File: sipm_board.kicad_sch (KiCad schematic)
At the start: 17 parts, among them J5 *, J6 *, Q3 MMBT5088LT1G, Q4 MMBT5088LT1G, U9 MICROFC-60035-SMT-TR1

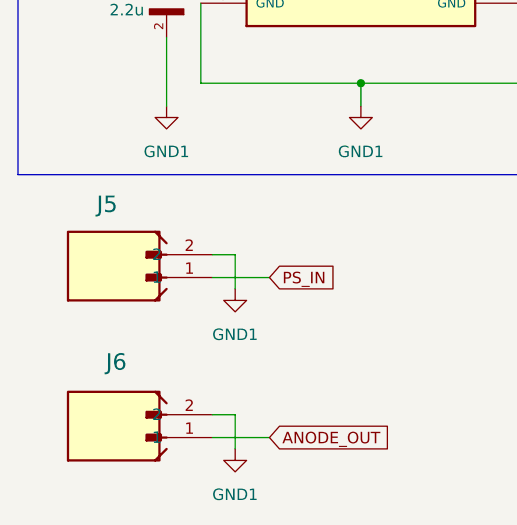
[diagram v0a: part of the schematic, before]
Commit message: Corrected labels
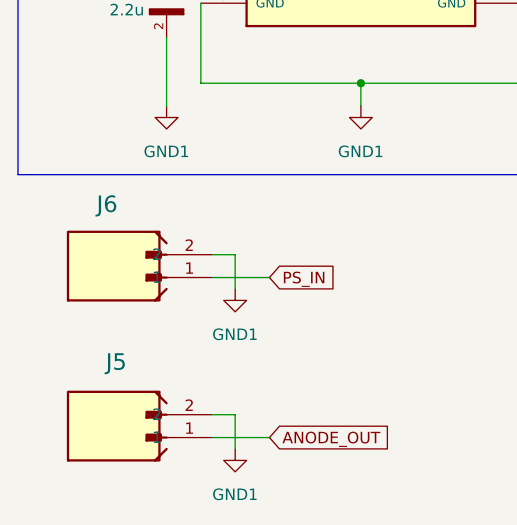
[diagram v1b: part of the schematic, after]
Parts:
- renumbered J6 to J5, J5 to J6
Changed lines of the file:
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@@
 		(on_board yes)
 		(dnp no)
-		(property "Reference" "J6"
+		(property "Reference" "J5"
 			(at 94.742 140.208 0)
 			(effects
@@
 			(project "gamma-spectrometer"
 				(path "/1fc9c372-472b-46ca-8d3b-f4aefe31a8be/1929b78d-718a-49ce-a44a-01f5c50b8f35"
-					(reference "J6")
+					(reference "J5")
 					(unit 1)
 				)
@@
 		(on_board yes)
 		(dnp no)
-		(property "Reference" "J5"
+		(property "Reference" "J6"
 			(at 93.726 122.682 0)
 			(effects
@@
 			(project "gamma-spectrometer"
 				(path "/1fc9c372-472b-46ca-8d3b-f4aefe31a8be/1929b78d-718a-49ce-a44a-01f5c50b8f35"
-					(reference "J5")
+					(reference "J6")
 					(unit 1)
 				)

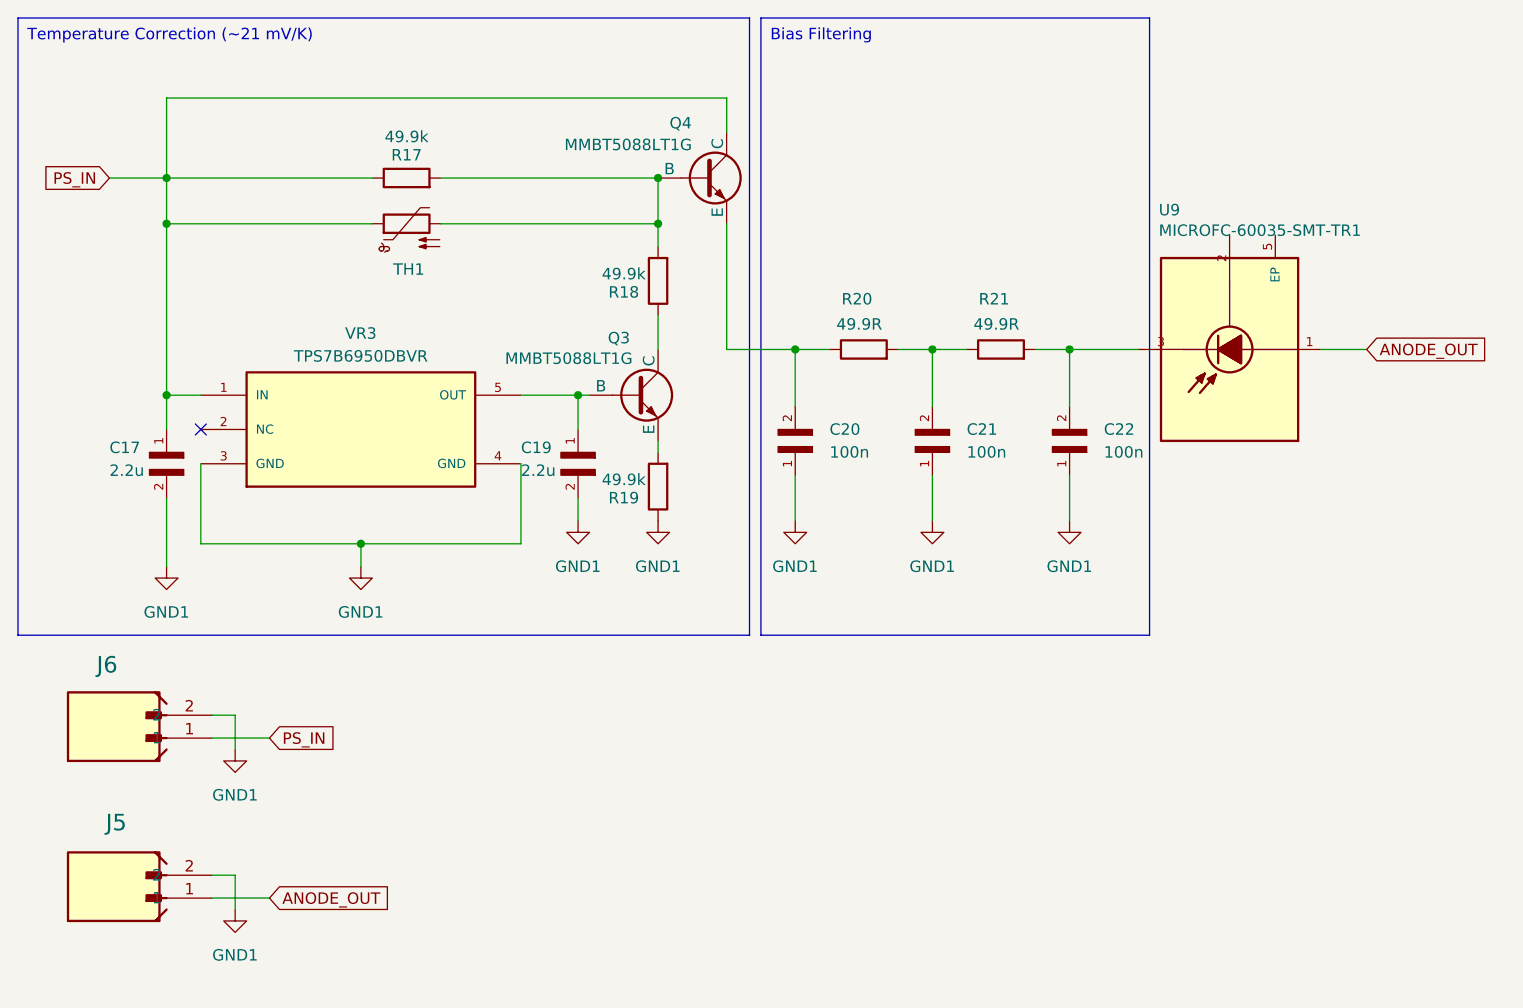
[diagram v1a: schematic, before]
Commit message: Added gain regulator. MHF3 connector for signal line.
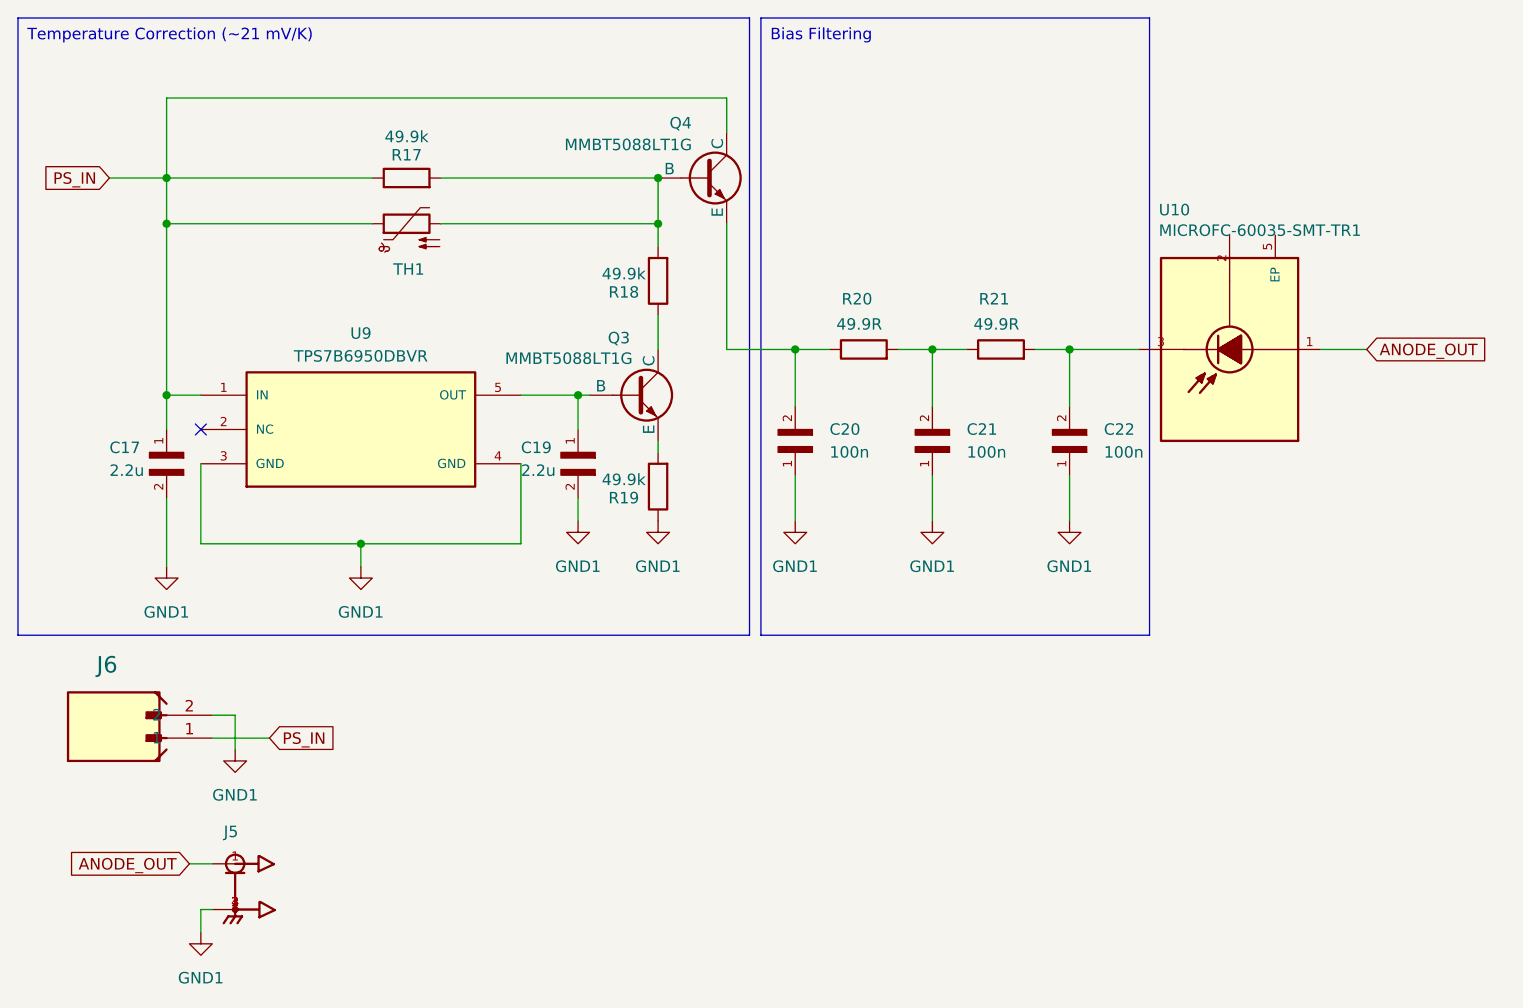
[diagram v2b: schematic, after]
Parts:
- removed J5: *, B2B-PH-K-S_LF__SN_:JST_B2B-PH-K-S(LF)(SN), symbol B2B-PH-K-S_LF__SN_:B2B-PH-K-S(LF)(SN)
- added J5: 20449-001E-03, 20449-001E-03:IPEX_20449-001E-03, symbol 20449-001E-03:20449-001E-03
- renumbered U9 to U10, VR3 to U9
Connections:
- net ANODE_OUT: now also J5.1
- net GND1: now also J5.2, J5.3, J5.4
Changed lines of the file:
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@@
+	(wire
+		(pts
+			(xy 102.87 144.78) (xy 105.41 144.78)
+		)
+		(stroke
+			(width 0)
+			(type default)
+		)
+	)
 	(wire
 		(pts
@@
 	(wire
 		(pts
-			(xy 107.95 146.05) (xy 107.95 149.86)
+			(xy 104.14 152.4) (xy 104.14 149.86)
 		)
 		(stroke
@@
 	(wire
 		(pts
-			(xy 111.76 148.59) (xy 105.41 148.59)
-		)
-		(stroke
-			(width 0)
-			(type default)
-		)
-	)
-	(wire
-		(pts
 			(xy 100.33 92.71) (xy 104.14 92.71)
 		)
@@
 	(wire
 		(pts
-			(xy 107.95 146.05) (xy 105.41 146.05)
-		)
-		(stroke
-			(width 0)
-			(type default)
-		)
-	)
-	(wire
-		(pts
 			(xy 200.66 87.63) (xy 208.28 87.63)
 		)
@@
 		(pts
 			(xy 104.14 109.22) (xy 121.92 109.22)
+		)
+		(stroke
+			(width 0)
+			(type default)
+		)
+	)
+	(wire
+		(pts
+			(xy 104.14 149.86) (xy 105.41 149.86)
 		)
 		(stroke
@@
 	(global_label "ANODE_OUT"
 		(shape input)
-		(at 111.76 148.59 0)
+		(at 102.87 144.78 180)
 		(fields_autoplaced yes)
 		(effects
@@
 				(size 1.27 1.27)
 			)
-			(justify left)
+			(justify right)
 		)
 		(property "Intersheetrefs" "${INTERSHEET_REFS}"
-			(at 125.51 148.59 0)
-			(effects
-				(font
-					(size 1.27 1.27)
-				)
-				(justify left)
+			(at 89.12 144.78 0)
+			(effects
+				(font
+					(size 1.27 1.27)
+				)
+				(justify right)
 				(hide yes)
 			)
@@
 				(justify left)
 				(hide yes)
+			)
+		)
+	)
+	(symbol
+		(lib_id "20449-001E-03:20449-001E-03")
+		(at 107.95 147.32 0)
+		(unit 1)
+		(exclude_from_sim no)
+		(in_bom yes)
+		(on_board yes)
+		(dnp no)
+		(property "Reference" "J5"
+			(at 106.68 141.224 0)
+			(effects
+				(font
+					(size 1.27 1.27)
+				)
+				(justify left)
+			)
+		)
+		(property "Value" "20449-001E-03"
+			(at 114.3 148.8439 0)
+			(effects
+				(font
+					(size 1.27 1.27)
+				)
+				(justify left)
+				(hide yes)
+			)
+		)
+		(property "Footprint" "20449-001E-03:IPEX_20449-001E-03"
+			(at 107.95 147.32 0)
+			(effects
+				(font
+					(size 1.27 1.27)
+				)
+				(justify bottom)
+				(hide yes)
+			)
+		)
+		(property "Datasheet" ""
+			(at 107.95 147.32 0)
+			(effects
+				(font
+					(size 1.27 1.27)
+				)
+				(hide yes)
+			)
+		)
+		(property "Description" ""
+			(at 107.95 147.32 0)
+			(effects
+				(font
+					(size 1.27 1.27)
+				)
+				(hide yes)
+			)
+		)
+		(property "MF" "I-PEX"
+			(at 107.95 147.32 0)
+			(effects
+				(font
+					(size 1.27 1.27)
+				)
+				(justify bottom)
+				(hide yes)
+			)
+		)
+		(property "Description_1" "\n                        \n                            1 POS Vertical SMD Small form factor with big performance through 6 GHz connector, RF, micro-coaxial MHF 4 Receptacle\n                        \n"
+			(at 107.95 147.32 0)
+			(effects
+				(font
+					(size 1.27 1.27)
+				)
+				(justify bottom)
+				(hide yes)
+			)
+		)
+		(property "Package" "None"
+			(at 107.95 147.32 0)
+			(effects
+				(font
+					(size 1.27 1.27)
+				)
+				(justify bottom)
+				(hide yes)
+			)
+		)
+		(property "Price" "None"
+			(at 107.95 147.32 0)
+			(effects
+				(font
+					(size 1.27 1.27)
+				)
+				(justify bottom)
+				(hide yes)
+			)
+		)
+		(property "Check_prices" "https://www.snapeda.com/parts/20449-001E-03/I-PEX/view-part/?ref=eda"
+			(at 107.95 147.32 0)
+			(effects
+				(font
+					(size 1.27 1.27)
+				)
+				(justify bottom)
+				(hide yes)
+			)
+		)
+		(property "PARTREV" "5"
+			(at 107.95 147.32 0)
+			(effects
+				(font
+					(size 1.27 1.27)
+				)
+				(justify bottom)
+				(hide yes)
+			)
+		)
+		(property "SnapEDA_Link" "https://www.snapeda.com/parts/20449-001E-03/I-PEX/view-part/?ref=snap"
+			(at 107.95 147.32 0)
+			(effects
+				(font
+					(size 1.27 1.27)
+				)
+				(justify bottom)
+				(hide yes)
+			)
+		)
+		(property "MP" "20449-001E-03"
+			(at 107.95 147.32 0)
+			(effects
+				(font
+					(size 1.27 1.27)
+				)
+				(justify bottom)
+				(hide yes)
+			)
+		)
+		(property "Availability" "In Stock"
+			(at 107.95 147.32 0)
+			(effects
+				(font
+					(size 1.27 1.27)
+				)
+				(justify bottom)
+				(hide yes)
+			)
+		)
+		(property "STANDART" "Manufacturer Recomendations"
+			(at 107.95 147.32 0)
+			(effects
+				(font
+					(size 1.27 1.27)
+				)
+				(justify bottom)
+				(hide yes)
+			)
+		)
+		(pin "4"
+		)
+		(pin "1"
+		)
+		(pin "3"
+		)
+		(pin "2"
+		)
+		(instances
+			(project ""
+				(path "/1fc9c372-472b-46ca-8d3b-f4aefe31a8be/1929b78d-718a-49ce-a44a-01f5c50b8f35"
+					(reference "J5")
+					(unit 1)
+				)
 			)
 		)
@@
 	(symbol
 		(lib_id "power:GND")
-		(at 107.95 149.86 0)
+		(at 104.14 152.4 0)
 		(unit 1)
 		(exclude_from_sim no)
@@
 		(fields_autoplaced yes)
 		(property "Reference" "#PWR072"
-			(at 107.95 156.21 0)
+			(at 104.14 158.75 0)
 			(effects
 				(font
@@
 		)
 		(property "Value" "GND1"
-			(at 107.95 154.94 0)
+			(at 104.14 157.48 0)
 			(effects
 				(font
@@
 		)
 		(property "Footprint" ""
-			(at 107.95 149.86 0)
+			(at 104.14 152.4 0)
 			(effects
 				(font
@@
 		)
 		(property "Datasheet" ""
-			(at 107.95 149.86 0)
+			(at 104.14 152.4 0)
 			(effects
 				(font
@@
 		)
 		(property "Description" "Power symbol creates a global label with name \"GND\" , ground"
-			(at 107.95 149.86 0)
+			(at 104.14 152.4 0)
 			(effects
 				(font
@@
 	)
 	(symbol
-		(lib_id "B2B-PH-K-S_LF__SN_:B2B-PH-K-S(LF)(SN)")
-		(at 95.25 146.05 180)
-		(unit 1)
-		(exclude_from_sim no)
-		(in_bom yes)
-		(on_board yes)
-		(dnp no)
-		(property "Reference" "J5"
-			(at 94.742 140.208 0)
-			(effects
-				(font
-					(size 1.8288 1.8288)
-				)
-			)
-		)
-		(property "Value" "*"
-			(at 94.853 140.97 0)
-			(effects
-				(font
-					(size 1.8288 1.8288)
-				)
-				(hide yes)
-			)
-		)
-		(property "Footprint" "B2B-PH-K-S_LF__SN_:JST_B2B-PH-K-S(LF)(SN)"
-			(at 95.25 146.05 0)
-			(effects
-				(font
-					(size 1.27 1.27)
-				)
-				(hide yes)
-			)
-		)
-		(property "Datasheet" ""
-			(at 95.25 146.05 0)
-			(effects
-				(font
-					(size 1.27 1.27)
-				)
-				(hide yes)
-			)
-		)
-		(property "Description" "Connector Header Through Hole 2 position 0.079 (2.00mm)"
-			(at 95.25 146.05 0)
-			(effects
-				(font
-					(size 1.27 1.27)
-				)
-				(hide yes)
-			)
-		)
-		(property "SnapEDA_Link" "https://www.snapeda.com/parts/B2B-PH-K-S%20(LF)(SN)/JST/view-part/?ref=snap"
-			(at 95.25 146.05 0)
-			(effects
-				(font
-					(size 1.8288 1.8288)
-				)
-				(justify left)
-				(hide yes)
-			)
-		)
-		(property "Package" "None"
-			(at 95.25 146.05 0)
-			(effects
-				(font
-					(size 1.8288 1.8288)
-				)
-				(justify left)
-				(hide yes)
-			)
-		)
-		(property "ALTIUM_VALUE" "*"
-			(at 95.25 146.05 0)
-			(effects
-				(font
-					(size 1.8288 1.8288)
-				)
-				(justify left)
-				(hide yes)
-			)
-		)
-		(property "MF" "JST"
-			(at 95.25 146.05 0)
-			(effects
-				(font
-					(size 1.8288 1.8288)
-				)
-				(justify left)
-				(hide yes)
-			)
-		)
-		(property "MP" "B2B-PH-K-S (LF)(SN)"
-			(at 95.25 146.05 0)
-			(effects
-				(font
-					(size 1.8288 1.8288)
-				)
-				(justify left)
-				(hide yes)
-			)
-		)
-		(property "Check_prices" "https://www.snapeda.com/parts/B2B-PH-K-S%20(LF)(SN)/JST/view-part/?ref=eda"
-			(at 95.25 146.05 0)
-			(effects
-				(font
-					(size 1.8288 1.8288)
-				)
-				(justify left)
-				(hide yes)
-			)
-		)
-		(pin "1"
-		)
-		(pin "2"
-		)
-		(instances
-			(project "gamma-spectrometer"
-				(path "/1fc9c372-472b-46ca-8d3b-f4aefe31a8be/1929b78d-718a-49ce-a44a-01f5c50b8f35"
-					(reference "J5")
-					(unit 1)
-				)
-			)
-		)
-	)
-	(symbol
 		(lib_id "Device:R")
 		(at 154.94 102.87 180)
@@
 		(on_board yes)
 		(dnp no)
-		(property "Reference" "U9"
+		(property "Reference" "U10"
 			(at 210.566 72.136 90)
 			(effects
@@
 			(project ""
 				(path "/1fc9c372-472b-46ca-8d3b-f4aefe31a8be/1929b78d-718a-49ce-a44a-01f5c50b8f35"
-					(reference "U9")
+					(reference "U10")
 					(unit 1)
 				)
@@
 		(on_board yes)
 		(dnp no)
-		(property "Reference" "VR3"
+		(property "Reference" "U9"
 			(at 121.92 85.852 0)
 			(effects
@@
 			(project ""
 				(path "/1fc9c372-472b-46ca-8d3b-f4aefe31a8be/1929b78d-718a-49ce-a44a-01f5c50b8f35"
-					(reference "VR3")
+					(reference "U9")
 					(unit 1)
 				)

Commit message: BDG4-01 module boards design
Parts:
- removed J5: 20449-001E-03, 20449-001E-03:IPEX_20449-001E-03, symbol 20449-001E-03:20449-001E-03
- removed J6: *, B2B-PH-K-S_LF__SN_:JST_B2B-PH-K-S(LF)(SN), symbol B2B-PH-K-S_LF__SN_:B2B-PH-K-S(LF)(SN)
